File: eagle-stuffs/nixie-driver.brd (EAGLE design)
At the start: 94.9 x 69.8 mm, 65 parts, among them IC1 74141N/K155ID1, IC2 74LS595N, IC3 TPS562209, IC4 NE555, Q1 MPSA92, Q10 2N2222, Q11 IRF840, Q12 2N2222, Q2 MPSA92, Q3 MPSA92, Q4 MPSA92, Q5 MPSA42, Q6 MPSA42, Q7 MPSA42, Q8 MPSA42, Q9 PN2907

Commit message: Updated something
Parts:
- R11: value 27 -> 56
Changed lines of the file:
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@@
 <attribute name="VALUE" x="48.5394" y="9.525" size="1.27" layer="27" ratio="10"/>
 </element>
-<element name="R11" library="resistor" package="0207/10" value="27" x="87.63" y="34.29" smashed="yes" rot="R90">
+<element name="R11" library="resistor" package="0207/10" value="56" x="87.63" y="34.29" smashed="yes" rot="R90">
 <attribute name="NAME" x="88.011" y="32.512" size="1.27" layer="25" ratio="10" rot="R90"/>
 <attribute name="VALUE" x="88.265" y="32.0294" size="1.27" layer="27" ratio="10" rot="R90"/>

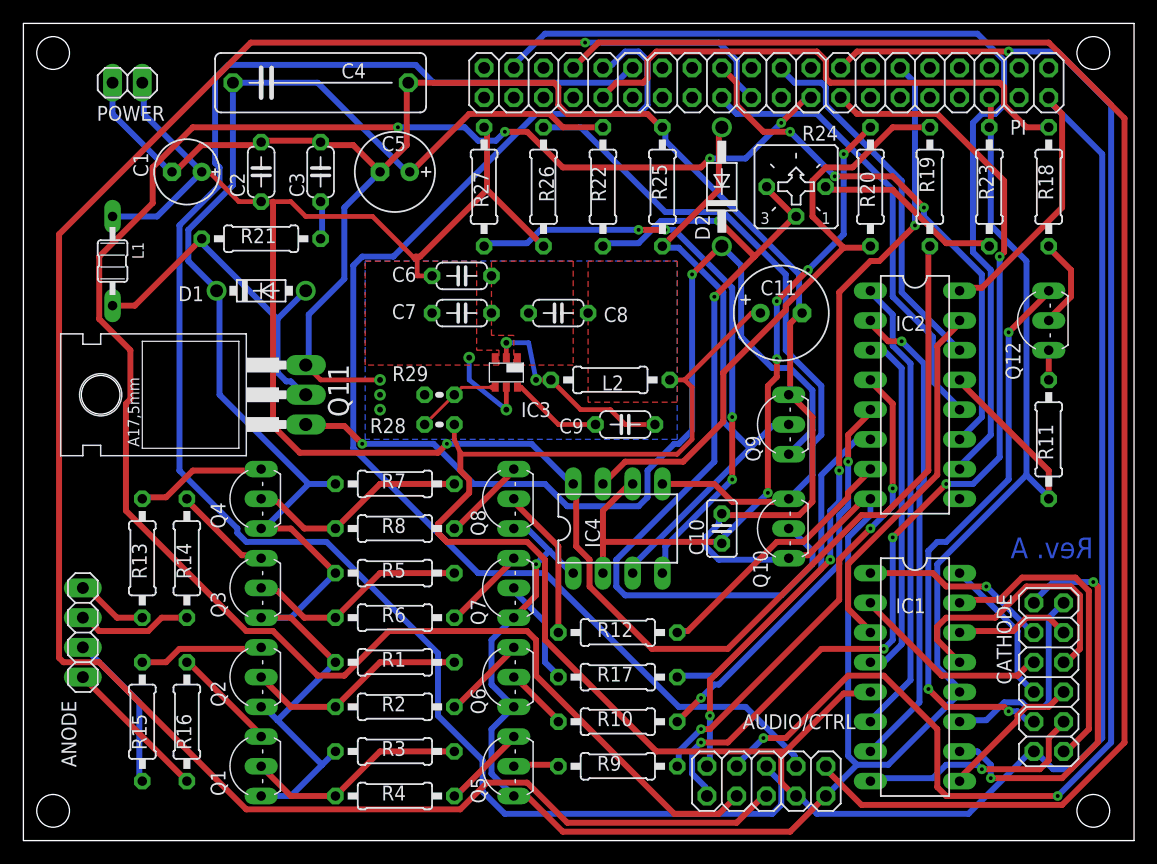
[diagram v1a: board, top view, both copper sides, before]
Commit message: Layout adjustement
Adjusted some physical component size & layout
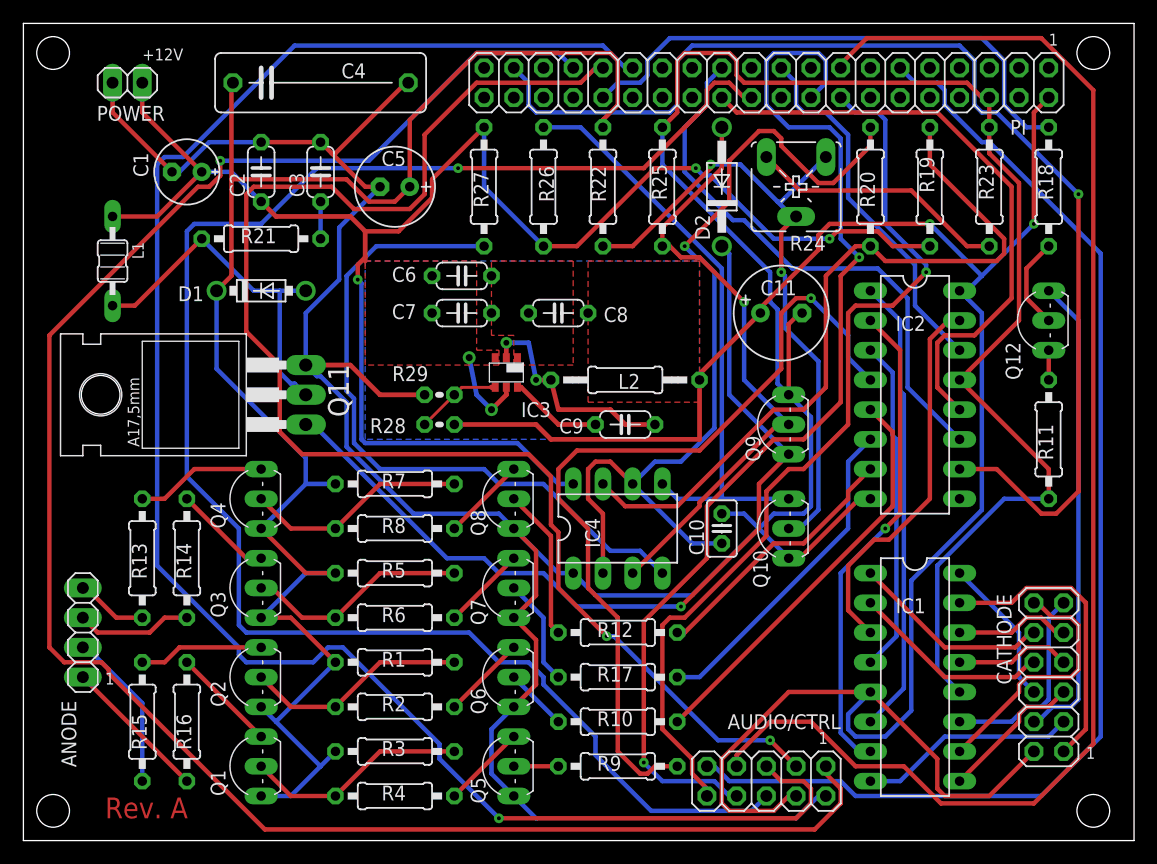
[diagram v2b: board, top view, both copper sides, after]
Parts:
- L2: device resistor:0207/10 -> resistor:0207/12
- R24: value 2K -> 2k; device pot:CT6 -> pot:CA6V
- moved L2 1.27 mm to (51.4, 39.4)
- moved C5 1.27 mm to (31.8, 55.9)
- turned R24 to 180 degrees
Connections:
- net N$64: now also R24.A; no longer R24.E
- net N$65: now also R24.E; no longer R24.A
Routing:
- net N$54: track 163.3 -> 92.9 mm, vias 4 -> 2
- net +12V: track 186.0 -> 146.8 mm, vias 3 -> 5
- net +5V: track 211.2 -> 175.7 mm, vias 0 -> 2
- net N$51: track 68.1 -> 102.6 mm, vias 4 -> 0
- net N$55: track 174.4 -> 143.8 mm
- net N$40: track 41.9 -> 71.9 mm, vias 3 -> 1
- net N$47: track 133.3 -> 161.6 mm, vias 0 -> 1
- net N$64: track 79.0 -> 57.3 mm
- net N$63: track 82.7 -> 101.0 mm, vias 0 -> 1
- net N$48: track 104.7 -> 122.2 mm, vias 0 -> 2
- net N$66: track 60.1 -> 76.9 mm, vias 5 -> 1
- net N$5: track 24.2 -> 9.94 mm
- net GND: track 328.6 -> 342.0 mm, vias 4 -> 0
- net N$41: track 39.1 -> 51.9 mm
- net N$8: track 34.4 -> 21.8 mm, vias 2 -> 0
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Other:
- board text added: "+12V"
- board text added: "1"

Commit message: Mirror cathod connector
Corrected major layout error!!! Needed to mirror cathod connector since
it mounted on bottom layer on lamp board and not on this board. Blowed
up my Pi this morning for the maiden test of the board :-(
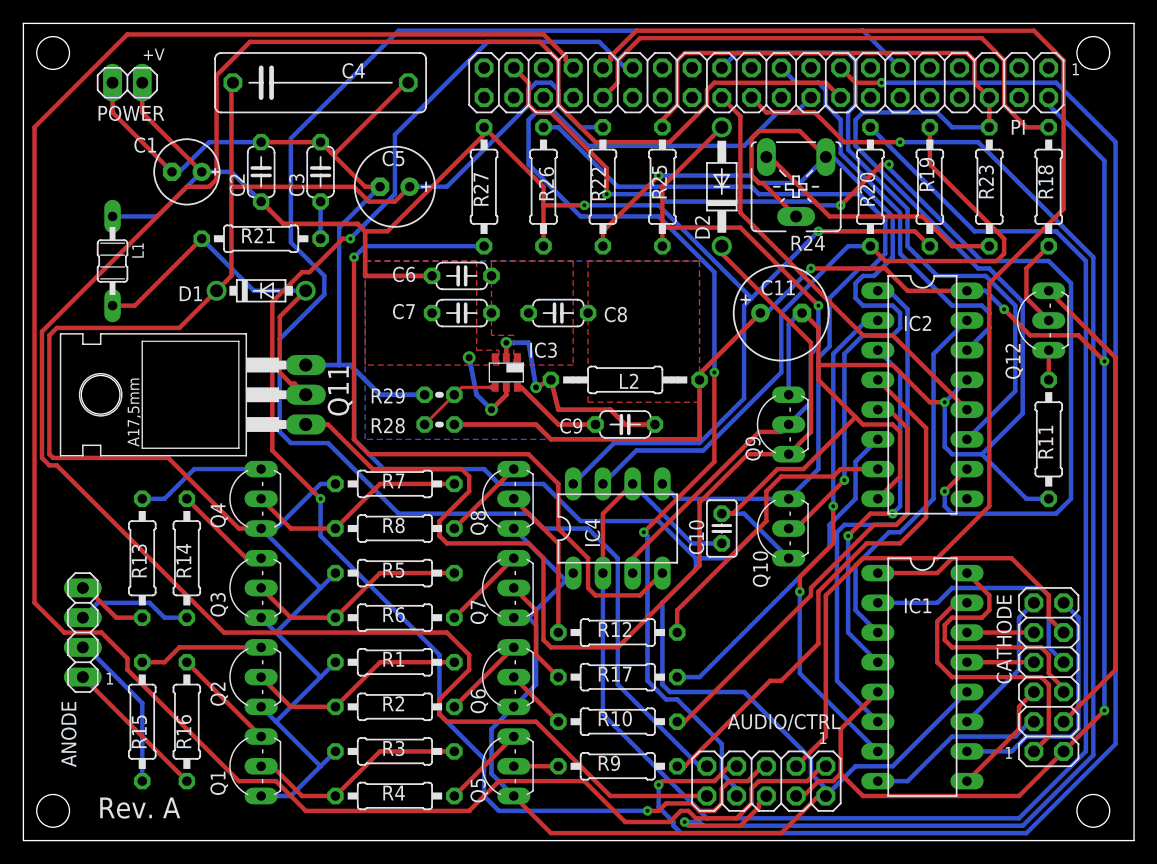
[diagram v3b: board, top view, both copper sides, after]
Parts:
- moved IC1 0.63 mm to (76.8, 14.0)
- moved IC2 0.63 mm to (76.8, 38.1)
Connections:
- net +5V: now also CATHODE.1; no longer CATHODE.2
- net N$10: now also CATHODE.7; no longer CATHODE.8
- net N$11: now also CATHODE.5; no longer CATHODE.6
- net N$2: now also CATHODE.2; no longer CATHODE.1
- net N$3: now also CATHODE.4; no longer CATHODE.3
- net N$4: now also CATHODE.6; no longer CATHODE.5
- net N$45: now also CATHODE.3; no longer CATHODE.4
- net N$5: now also CATHODE.8; no longer CATHODE.7
- net N$6: now also CATHODE.10; no longer CATHODE.9
- net N$7: now also CATHODE.12; no longer CATHODE.11
- net N$8: now also CATHODE.11; no longer CATHODE.12
- net N$9: now also CATHODE.9; no longer CATHODE.10
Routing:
- net N$53: track 78.1 -> 179.0 mm, vias 1 -> 0
- net N$66: track 76.9 -> 142.8 mm, vias 1 -> 0
- net GND: track 342.0 -> 388.5 mm, vias 0 -> 1
- net N$51: track 102.6 -> 139.7 mm
- net N$49: track 153.3 -> 121.1 mm, vias 1 -> 3
- net N$64: track 57.3 -> 84.7 mm
- net N$40: track 71.9 -> 46.1 mm, vias 1 -> 0
- net N$55: track 143.8 -> 123.3 mm, vias 1 -> 2
- net N$60: track 51.2 -> 71.6 mm
- net N$62: track 75.5 -> 91.6 mm, vias 1 -> 0
- net +24V: track 141.0 -> 156.1 mm
- net N$41: track 51.9 -> 36.8 mm
- net +5V: track 175.7 -> 162.3 mm, vias 2 -> 4
- net N$50: track 118.2 -> 130.1 mm, vias 0 -> 2
- net N$47: track 161.6 -> 172.6 mm, vias 1 -> 0
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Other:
- board text added: "+V"
- board text removed: "+12V"

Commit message: Updated to rev. b
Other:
- board text added: "Rev. B"
- board text removed: "Rev. A"
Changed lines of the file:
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@@
 <text x="67.945" y="8.255" size="1.016" layer="21">1</text>
 <text x="10.16" y="66.675" size="1.016" layer="21">+V</text>
-<text x="6.35" y="1.905" size="1.778" layer="21">Rev. A</text>
+<text x="6.35" y="1.905" size="1.778" layer="21">Rev. B</text>
 </plain>
 <attributes>

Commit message: Added some info
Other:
- board text added: "2"
- board text added: "4"
- board text added: "8"
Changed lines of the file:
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@@
 <text x="89.535" y="65.405" size="1.016" layer="21">1</text>
 <text x="83.82" y="6.985" size="1.016" layer="21">1</text>
-<text x="6.985" y="13.335" size="1.016" layer="21">1</text>
+<text x="7.62" y="18.415" size="1.016" layer="21">4</text>
 <text x="67.945" y="8.255" size="1.016" layer="21">1</text>
 <text x="10.16" y="66.675" size="1.016" layer="21">+V</text>
 <text x="6.35" y="1.905" size="1.778" layer="21">Rev. B</text>
+<text x="7.62" y="15.875" size="1.016" layer="21">2</text>
+<text x="7.62" y="13.335" size="1.016" layer="21">1</text>
+<text x="7.62" y="20.955" size="1.016" layer="21">8</text>
 </plain>
 <attributes>

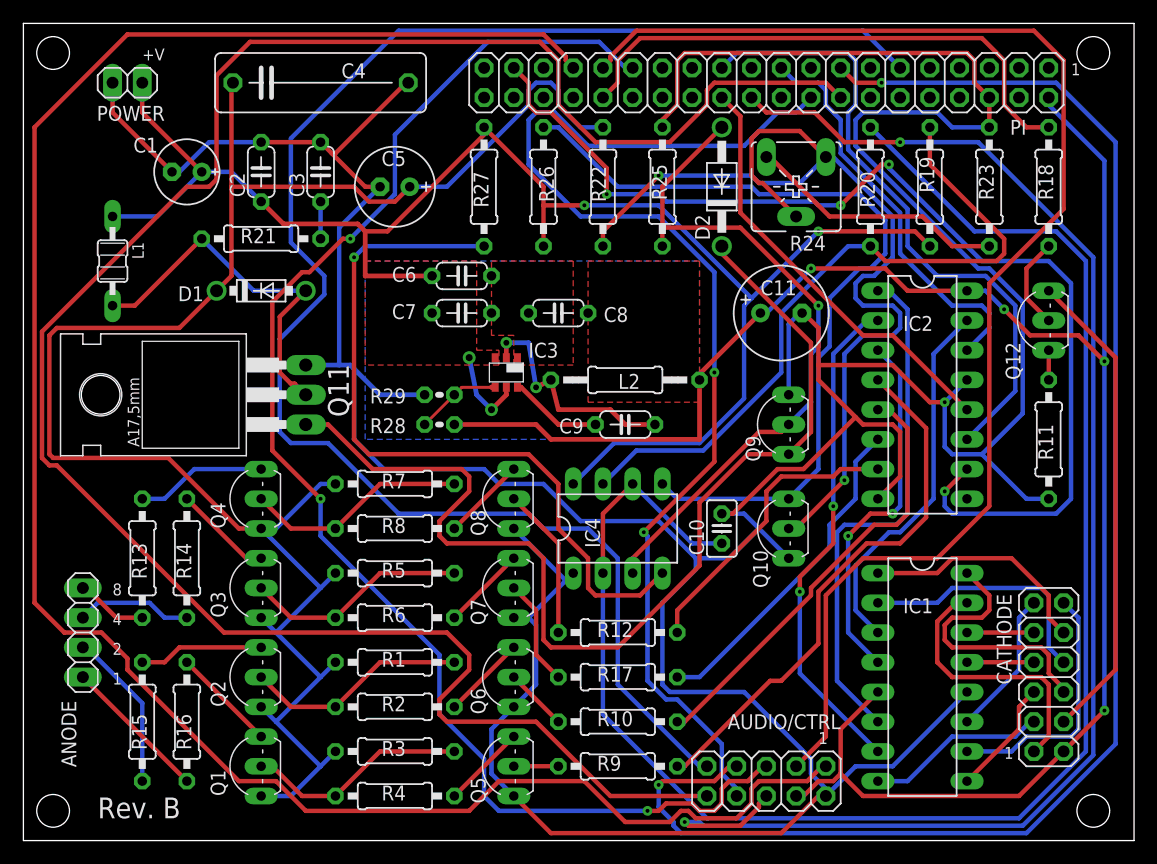
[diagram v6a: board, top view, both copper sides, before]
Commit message: Discarded the TPS562209
Too sensitive to touch (touching the chip, blow-it up!
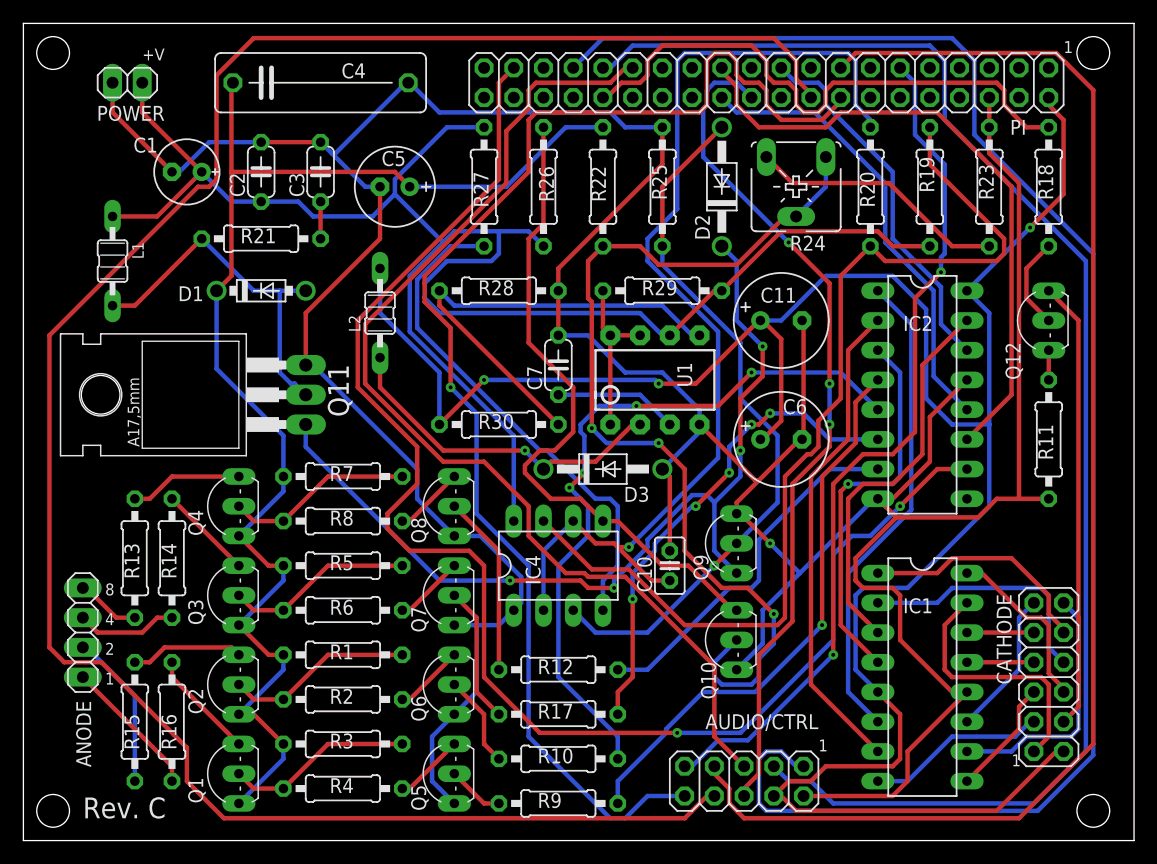
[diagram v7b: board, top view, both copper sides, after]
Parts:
- removed C8: 22, rcl:C050-024X044
- removed C9: 0.1, rcl:C050-024X044
- removed IC3: TPS562209, texas:TSOT23-6_DDC
- added D3: 1N5819, diode:DO41-10
- added R30: 3.6k, resistor:0207/10
- added U1: MC34063DIP, SparkFun-PowerIC:DIP-08
- C6: value 0.1 -> 470; device rcl:C050-024X044 -> rcl:E3,5-8
- C7: value 22 -> 470pF
- L2: value 4.7uH/1.7A -> 100uH/1A; device resistor:0207/12 -> inductors:MMICC7
- R28: value 59.4k -> 1.2k; device resistor:0204V -> resistor:0207/10
- R29: value 10k -> 0.33; device resistor:0204V -> resistor:0207/10
- moved C6 30.7 mm to (64.8, 34.3)
- moved L2 21.7 mm to (30.5, 45.1), turned to 90 degrees
- moved R29 21.0 mm to (54.6, 47.0)
- moved R28 12.5 mm to (40.6, 47.0)
- moved Q9 11.1 mm to (61.0, 25.4)
- moved Q10 10.5 mm to (59.7, 17.1)
- moved C7 9.38 mm to (45.7, 40.6), turned to 90 degrees
- moved IC4 5.99 mm to (45.7, 23.5)
- moved R10 5.99 mm to (45.7, 6.99)
- moved R12 5.99 mm to (45.7, 14.6)
- moved R17 5.99 mm to (45.7, 10.8)
- moved R9 5.99 mm to (45.7, 3.17)
- moved C10 5.46 mm to (55.2, 23.5)
- moved Q5 5.12 mm to (35.6, 5.71)
- moved Q6 5.12 mm to (35.6, 13.3)
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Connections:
- removed net SW: C9.1, IC3.2, L2.2
- removed net VBST: C9.2, IC3.6
- removed net VFB: IC3.4, R28.1, R29.2
- new net N$57: R29.1, U1.1, U1.7, U1.8
- new net N$67: R28.1, R30.2, U1.5
- new net N$68: C7.1, U1.3
- new net N$69: D3.C, L2.1, U1.2
- net +12V: now also R29.2, U1.6; no longer C6.1, C7.1, IC3.3, IC3.5
- net +5V: now also C6.+, L2.2, R30.1; no longer C8.1, L2.1, R28.2
- net GND: now also C6.-, D3.A, R28.2, U1.4; no longer C6.2, C8.2, IC3.1, R29.1
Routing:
- net N$54: track 101.9 -> 176.1 mm, vias 2 -> 0
- net N$51: track 139.7 -> 73.8 mm, vias 0 -> 2
- net N$53: track 179.0 -> 113.2 mm, vias 0 -> 1
- net N$66: track 142.8 -> 90.3 mm, vias 0 -> 1
- net N$55: track 123.3 -> 72.6 mm, vias 2 -> 3
- net GND: track 388.5 -> 343.8 mm
- net +24V: track 156.1 -> 112.3 mm
- net N$67: track 0.00 -> 39.4 mm
- net +5V: track 162.3 -> 198.6 mm, vias 4 -> 3
- net N$47: track 172.6 -> 138.9 mm
- net N$49: track 121.1 -> 91.5 mm, vias 3 -> 0
- net N$63: track 94.7 -> 124.0 mm, vias 4 -> 2
- net N$69: track 0.00 -> 29.2 mm, vias 0 -> 1
- net N$52: track 59.9 -> 85.2 mm
- net N$39: track 37.9 -> 61.6 mm, vias 0 -> 4
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- removed copper zone on layer 1, net +12V
- removed copper zone on layer 1, net +5V
- removed copper zone on layer 1, net GND
- removed copper zone on layer 16, net GND
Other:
- board text added: "Rev. C"
- board text removed: "Rev. B"

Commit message: Ajusted layout + add backplane shield
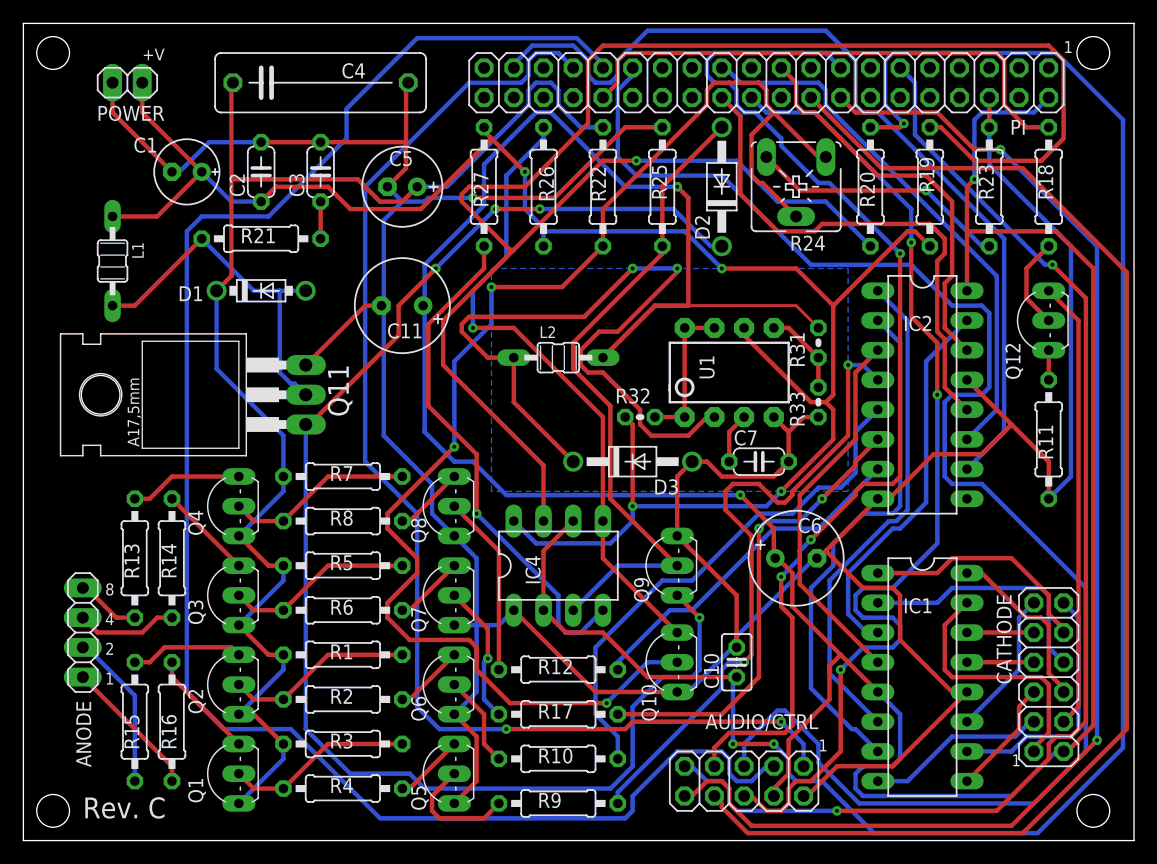
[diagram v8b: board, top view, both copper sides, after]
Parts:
- removed R28: 1.2k, resistor:0207/10
- removed R29: 0.33, resistor:0207/10
- removed R30: 3.6k, resistor:0207/10
- added R31: 3.6k, resistor:0204V
- added R32: 0.22, resistor:0204V
- added R33: 1.1k, resistor:0204V
- moved C11 32.4 mm to (32.4, 45.7), turned to 180 degrees
- moved C7 19.0 mm to (62.9, 32.4), turned to 0 degrees
- moved L2 15.7 mm to (45.7, 41.3), turned to 0 degrees
- moved C6 10.2 mm to (66.0, 24.1)
- moved C10 10.0 mm to (61.0, 15.2)
- moved U1 6.38 mm to (60.3, 40.0)
- moved Q10 5.43 mm to (54.6, 15.2)
- moved Q9 5.43 mm to (55.9, 23.5)
- moved D3 2.62 mm to (52.1, 32.4)
- moved C5 0.63 mm to (32.4, 55.9)
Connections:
- net +12V: now also R32.1; no longer R29.2
- net +5V: now also R31.2; no longer R30.1
- net GND: now also R33.1; no longer R28.2
- net N$57: now also R32.2; no longer R29.1
- net N$67: now also R31.1, R33.2; no longer R28.1, R30.2
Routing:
- net N$66: track 90.3 -> 159.3 mm, vias 1 -> 3
- net N$52: track 85.2 -> 153.1 mm, vias 0 -> 1
- net N$54: track 176.1 -> 112.6 mm
- net +5V: track 198.6 -> 251.6 mm
- net N$63: track 124.0 -> 78.1 mm, vias 2 -> 0
- net N$62: track 78.0 -> 122.1 mm
- net N$49: track 91.5 -> 130.8 mm
- net N$69: track 29.2 -> 65.3 mm, vias 1 -> 2
- net N$64: track 81.7 -> 117.6 mm
- net N$47: track 138.9 -> 106.8 mm, vias 0 -> 2
- net N$67: track 39.4 -> 7.40 mm
- net N$51: track 73.8 -> 103.3 mm
- net GND: track 343.8 -> 317.6 mm
- net N$50: track 117.3 -> 92.9 mm, vias 0 -> 3
- net N$48: track 124.4 -> 144.6 mm
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- added copper zone on layer 16, net GND
